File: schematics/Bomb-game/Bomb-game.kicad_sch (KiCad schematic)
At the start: 9 parts, among them J1 Joystick, U1 ADKeyboard, U2 Relays x4, U3 Emergency Button, U4 Buzzer, U5 Buzzer, U6 8x8 WS2812B, U7 LCD 1602

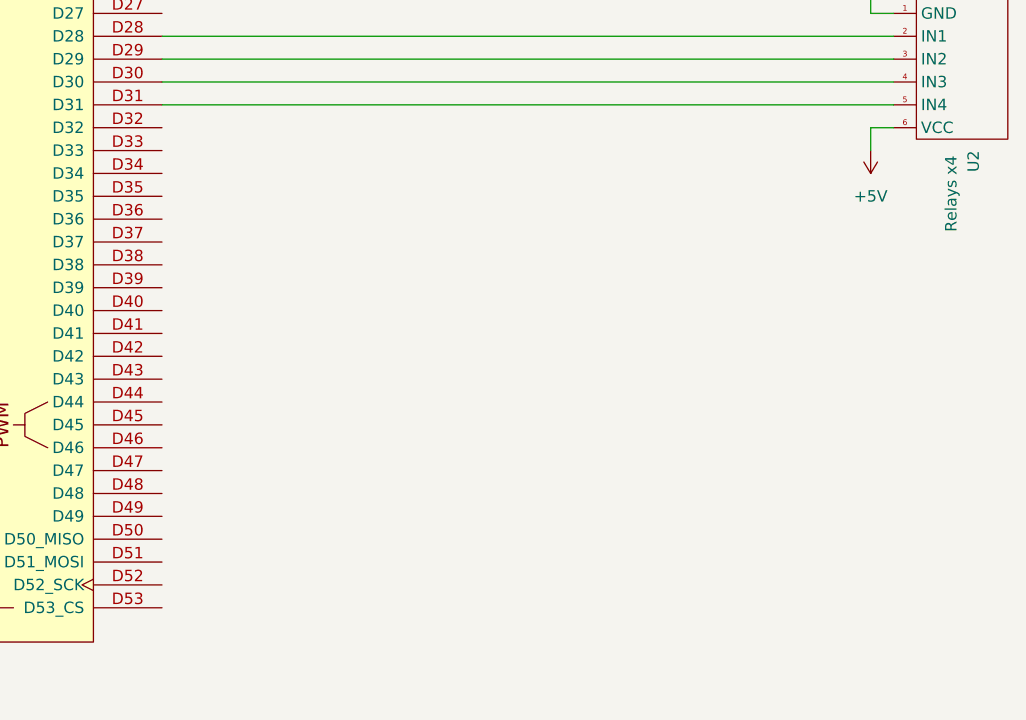
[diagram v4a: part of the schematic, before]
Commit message: Add 3x4 keyboard to schematics
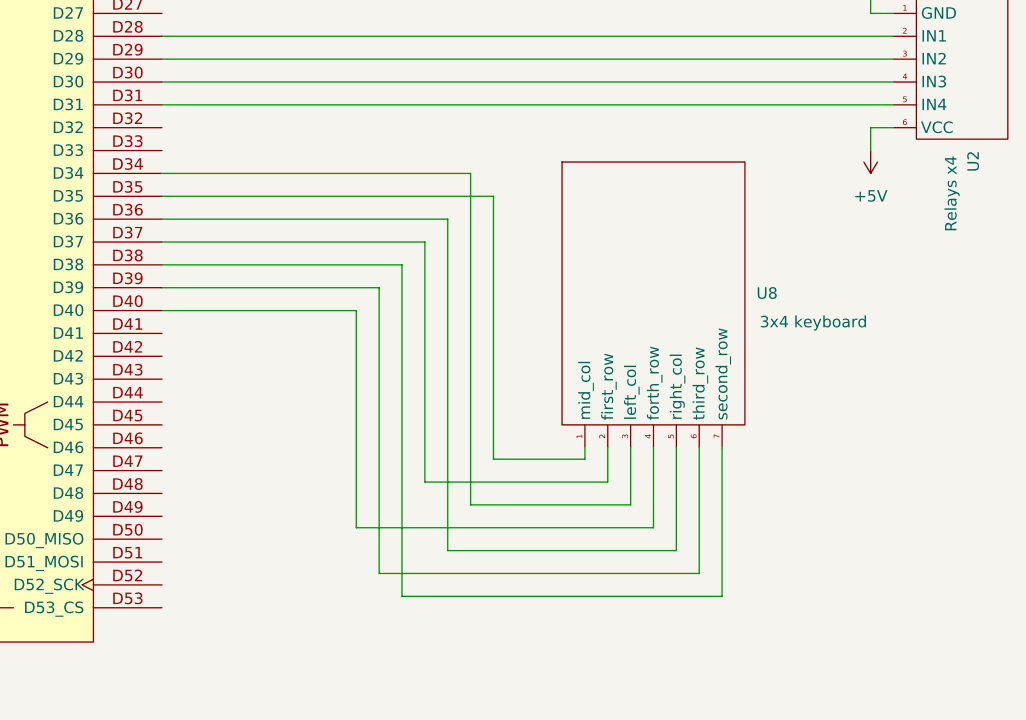
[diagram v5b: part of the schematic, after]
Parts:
- added U8: 3x4 keyboard, symbol Bomb-parts:3x4_keyboard
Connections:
- net at XA1.D34: now also U8.3 (left_col)
- net at XA1.D35: now also U8.1 (mid_col)
- net at XA1.D36: now also U8.5 (right_col)
- net at XA1.D37: now also U8.2 (first_row)
- net at XA1.D38: now also U8.7 (second_row)
- net at XA1.D39: now also U8.6 (third_row)
- net at XA1.D40: now also U8.4 (forth_row)
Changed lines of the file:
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@@
   )
   (no_connect (at 223.52 58.42))
+  (wire (pts (xy 207.01 105.41) (xy 175.26 105.41))
+    (stroke (width 0) (type default))
+  )
+  (wire (pts (xy 229.87 130.81) (xy 229.87 139.7))
+    (stroke (width 0) (type default))
+  )
+  (wire (pts (xy 234.95 144.78) (xy 199.39 144.78))
+    (stroke (width 0) (type default))
+  )
   (wire (pts (xy 73.66 88.9) (xy 73.66 77.47))
     (stroke (width 0) (type default))
@@
     (stroke (width 0) (type default))
   )
+  (wire (pts (xy 222.25 130.81) (xy 222.25 132.08))
+    (stroke (width 0) (type default))
+  )
   (wire (pts (xy 254 80.01) (xy 254 82.55))
     (stroke (width 0) (type default))
@@
     (stroke (width 0) (type default))
   )
+  (wire (pts (xy 196.85 115.57) (xy 175.26 115.57))
+    (stroke (width 0) (type default))
+  )
+  (wire (pts (xy 209.55 137.16) (xy 209.55 100.33))
+    (stroke (width 0) (type default))
+  )
   (wire (pts (xy 254 95.25) (xy 254 97.79))
     (stroke (width 0) (type default))
   )
+  (wire (pts (xy 199.39 113.03) (xy 175.26 113.03))
+    (stroke (width 0) (type default))
+  )
   (wire (pts (xy 57.15 76.2) (xy 59.69 76.2))
     (stroke (width 0) (type default))
   )
+  (wire (pts (xy 212.09 132.08) (xy 212.09 102.87))
+    (stroke (width 0) (type default))
+  )
   (wire (pts (xy 87.63 52.07) (xy 87.63 58.42))
     (stroke (width 0) (type default))
@@
     (stroke (width 0) (type default))
   )
+  (wire (pts (xy 227.33 137.16) (xy 209.55 137.16))
+    (stroke (width 0) (type default))
+  )
   (wire (pts (xy 105.41 133.35) (xy 105.41 130.81))
     (stroke (width 0) (type default))
@@
     (stroke (width 0) (type default))
   )
+  (wire (pts (xy 237.49 147.32) (xy 201.93 147.32))
+    (stroke (width 0) (type default))
+  )
+  (wire (pts (xy 204.47 134.62) (xy 204.47 107.95))
+    (stroke (width 0) (type default))
+  )
   (wire (pts (xy 199.39 59.69) (xy 175.26 59.69))
     (stroke (width 0) (type default))
@@
     (stroke (width 0) (type default))
   )
+  (wire (pts (xy 234.95 130.81) (xy 234.95 144.78))
+    (stroke (width 0) (type default))
+  )
   (wire (pts (xy 109.22 140.97) (xy 109.22 143.51))
     (stroke (width 0) (type default))
@@
     (stroke (width 0) (type default))
   )
+  (wire (pts (xy 222.25 132.08) (xy 212.09 132.08))
+    (stroke (width 0) (type default))
+  )
   (wire (pts (xy 203.2 55.88) (xy 203.2 58.42))
     (stroke (width 0) (type default))
@@
     (stroke (width 0) (type default))
   )
+  (wire (pts (xy 209.55 100.33) (xy 175.26 100.33))
+    (stroke (width 0) (type default))
+  )
   (wire (pts (xy 106.68 148.59) (xy 109.22 148.59))
     (stroke (width 0) (type default))
@@
     (stroke (width 0) (type default))
   )
+  (wire (pts (xy 207.01 142.24) (xy 207.01 105.41))
+    (stroke (width 0) (type default))
+  )
   (wire (pts (xy 76.2 91.44) (xy 76.2 80.01))
     (stroke (width 0) (type default))
@@
     (stroke (width 0) (type default))
   )
+  (wire (pts (xy 201.93 110.49) (xy 175.26 110.49))
+    (stroke (width 0) (type default))
+  )
   (wire (pts (xy 175.26 85.09) (xy 256.54 85.09))
     (stroke (width 0) (type default))
   )
+  (wire (pts (xy 227.33 130.81) (xy 227.33 137.16))
+    (stroke (width 0) (type default))
+  )
   (wire (pts (xy 78.74 52.07) (xy 87.63 52.07))
     (stroke (width 0) (type default))
@@
     (stroke (width 0) (type default))
   )
+  (wire (pts (xy 199.39 144.78) (xy 199.39 113.03))
+    (stroke (width 0) (type default))
+  )
   (wire (pts (xy 256.54 95.25) (xy 254 95.25))
     (stroke (width 0) (type default))
@@
     (stroke (width 0) (type default))
   )
+  (wire (pts (xy 224.79 134.62) (xy 204.47 134.62))
+    (stroke (width 0) (type default))
+  )
   (wire (pts (xy 97.79 46.99) (xy 97.79 62.23))
     (stroke (width 0) (type default))
   )
+  (wire (pts (xy 232.41 130.81) (xy 232.41 142.24))
+    (stroke (width 0) (type default))
+  )
+  (wire (pts (xy 237.49 130.81) (xy 237.49 147.32))
+    (stroke (width 0) (type default))
+  )
   (wire (pts (xy 62.23 88.9) (xy 73.66 88.9))
     (stroke (width 0) (type default))
   )
+  (wire (pts (xy 224.79 130.81) (xy 224.79 134.62))
+    (stroke (width 0) (type default))
+  )
+  (wire (pts (xy 196.85 139.7) (xy 196.85 115.57))
+    (stroke (width 0) (type default))
+  )
   (wire (pts (xy 223.52 66.04) (xy 227.33 66.04))
     (stroke (width 0) (type default))
@@
     (stroke (width 0) (type default))
   )
+  (wire (pts (xy 201.93 147.32) (xy 201.93 110.49))
+    (stroke (width 0) (type default))
+  )
   (wire (pts (xy 62.23 99.06) (xy 67.31 99.06))
     (stroke (width 0) (type default))
@@
     (stroke (width 0) (type default))
   )
+  (wire (pts (xy 212.09 102.87) (xy 175.26 102.87))
+    (stroke (width 0) (type default))
+  )
   (wire (pts (xy 223.52 62.23) (xy 226.06 62.23))
     (stroke (width 0) (type default))
@@
   )
   (wire (pts (xy 78.74 49.53) (xy 95.25 49.53))
+    (stroke (width 0) (type default))
+  )
+  (wire (pts (xy 204.47 107.95) (xy 175.26 107.95))
+    (stroke (width 0) (type default))
+  )
+  (wire (pts (xy 232.41 142.24) (xy 207.01 142.24))
+    (stroke (width 0) (type default))
+  )
+  (wire (pts (xy 229.87 139.7) (xy 196.85 139.7))
     (stroke (width 0) (type default))
   )
@@
         )
       )
+    )
+  )
+  (symbol (lib_id "Bomb-parts:3x4_keyboard") (at 229.87 114.3 0) (unit 1)
+    (in_bom yes) (on_board yes) (dnp no)
+    (property "Reference" "U8" (at 241.3 113.665 0)
+      (effects (font (size 1.27 1.27)) (justify left))
+    )
+    (property "Value" "3x4 keyboard" (at 247.65 116.84 0)
+      (effects (font (size 1.27 1.27)))
+    )
+    (property "Footprint" "" (at 229.87 114.3 0)
+      (effects (font (size 1.27 1.27)) hide)
+    )
+    (property "Datasheet" "" (at 229.87 114.3 0)
+      (effects (font (size 1.27 1.27)) hide)
+    )
+    (pin "1")
+    (pin "2")
+    (pin "3")
+    (pin "4")
+    (pin "5")
+    (pin "6")
+    (pin "7")
+    (instances
+      (project "Bomb-game"
+        (path "/d5dfcc17-2f57-46e4-9b81-9957aca5a4a9"
+          (reference "U8") (unit 1)
+        )
+      )

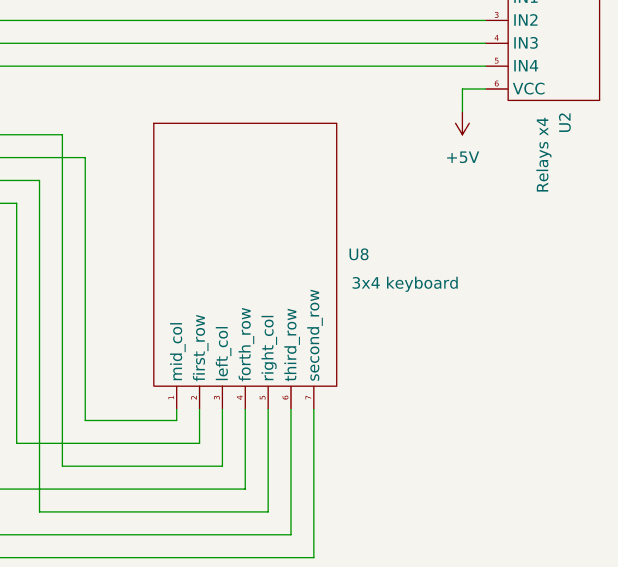
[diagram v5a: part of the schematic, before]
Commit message: Fix redefinition of button states
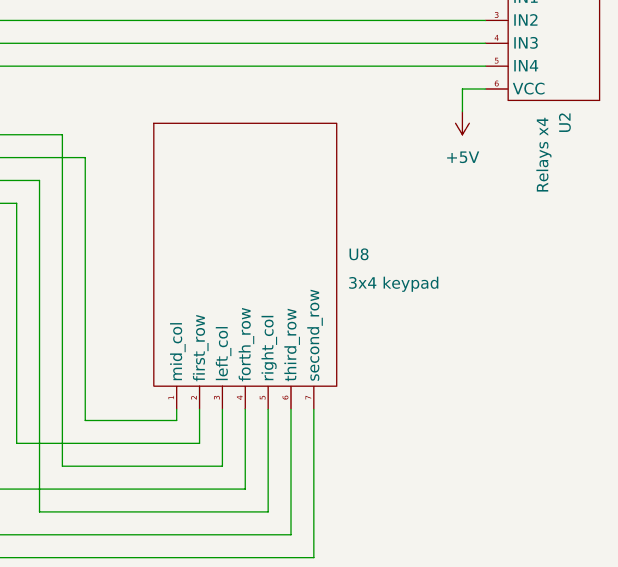
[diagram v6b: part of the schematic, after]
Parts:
- U8: value 3x4 keyboard -> 3x4 keypad
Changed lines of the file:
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@@
       (effects (font (size 1.27 1.27)) (justify left))
     )
-    (property "Value" "3x4 keyboard" (at 247.65 116.84 0)
+    (property "Value" "3x4 keypad" (at 246.38 116.84 0)
       (effects (font (size 1.27 1.27)))
     )
